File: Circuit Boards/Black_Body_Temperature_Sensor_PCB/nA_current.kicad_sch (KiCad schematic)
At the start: 12 parts, among them Q7 TMUX1112PWR, U2 LM334M, U3 LT1008

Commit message: power simulation
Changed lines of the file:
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@@
-		)
-	)
-	(label "\"sel\"{100na_neg 100na_pos 10na_neg 10na_pos}"
-		(at 162.56 120.65 90)
-		(effects
-			(font
-				(size 0.2 0.2)
-			)
-			(justify left bottom)
 		)
 	)

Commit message: Schematic ready for review
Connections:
- net +4V renamed +3V3A
- net -4V renamed -3V3A

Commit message: Temp sensor schematic done
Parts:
- C301: renamed from C1; footprint (none) -> Capacitor_SMD:C_0603_1608Metric
- R301: renamed from R12; footprint (none) -> Resistor_SMD:R_0603_1608Metric
- R302: renamed from R13; footprint (none) -> Resistor_SMD:R_0603_1608Metric
- R303: renamed from R14; footprint (none) -> Resistor_SMD:R_0603_1608Metric
- R304: renamed from R11; footprint (none) -> Resistor_SMD:R_0603_1608Metric
- R305: renamed from R9; footprint (none) -> Resistor_SMD:R_0603_1608Metric
- R306: renamed from R10; footprint (none) -> Resistor_SMD:R_0603_1608Metric
- R307: renamed from R15; footprint (none) -> Resistor_SMD:R_0603_1608Metric
- renumbered D1 to D301, Q7 to Q301, U2 to U301, U3 to U302
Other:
- note added: "nA Current (PAGE 3)"
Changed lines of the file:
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@@
 	(generator_version "10.0")
 	(paper "A4")
+	(text "nA Current (PAGE 3)"
+		(exclude_from_sim no)
+		(at 69.85 24.13 0)
+		(effects
+			(font
+				(size 7 7)
+			)
+		)
+	)
 	(junction
 		(at 83.82 82.55)
@@
 		(dnp no)
 		(fields_autoplaced yes)
-		(property "Reference" "R9"
+		(property "Reference" "R305"
 			(at 105.41 76.1999 0)
 			(show_name no)
@@
 			)
 		)
-		(property "Footprint" ""
+		(property "Footprint" "Resistor_SMD:R_0603_1608Metric"
 			(at 101.092 77.47 90)
 			(hide yes)
@@
 			(project "Black_Body_Temperature_Sensor_PCB"
 				(path "/e46fba8d-0294-4f4f-927d-8614bb9d51d3/c0a0512b-fc86-46bb-aa4c-7d38a9ff5302"
-					(reference "R9")
+					(reference "R305")
 					(unit 1)
 				)
@@
 		(dnp no)
 		(fields_autoplaced yes)
-		(property "Reference" "R12"
+		(property "Reference" "R301"
 			(at 78.74 86.3599 0)
 			(show_name no)
@@
 			)
 		)
-		(property "Footprint" ""
+		(property "Footprint" "Resistor_SMD:R_0603_1608Metric"
 			(at 74.422 87.63 90)
 			(hide yes)
@@
 			(project "Black_Body_Temperature_Sensor_PCB"
 				(path "/e46fba8d-0294-4f4f-927d-8614bb9d51d3/c0a0512b-fc86-46bb-aa4c-7d38a9ff5302"
-					(reference "R12")
+					(reference "R301")
 					(unit 1)
 				)
@@
 		(dnp no)
 		(fields_autoplaced yes)
-		(property "Reference" "R13"
+		(property "Reference" "R302"
 			(at 86.36 76.1999 0)
 			(show_name no)
@@
 			)
 		)
-		(property "Footprint" ""
+		(property "Footprint" "Resistor_SMD:R_0603_1608Metric"
 			(at 82.042 77.47 90)
 			(hide yes)
@@
 			(project "Black_Body_Temperature_Sensor_PCB"
 				(path "/e46fba8d-0294-4f4f-927d-8614bb9d51d3/c0a0512b-fc86-46bb-aa4c-7d38a9ff5302"
-					(reference "R13")
+					(reference "R302")
 					(unit 1)
 				)
@@
 		(in_pos_files yes)
 		(dnp no)
-		(property "Reference" "C1"
-			(at 167.64 105.41 90)
+		(property "Reference" "C301"
+			(at 168.91 107.95 90)
 			(show_name no)
 			(do_not_autoplace no)
@@
 		)
 		(property "Value" "200pf"
-			(at 167.64 107.95 90)
-			(show_name no)
-			(do_not_autoplace no)
-			(effects
-				(font
-					(size 1.27 1.27)
-				)
-			)
-		)
-		(property "Footprint" ""
+			(at 168.91 110.49 90)
+			(show_name no)
+			(do_not_autoplace no)
+			(effects
+				(font
+					(size 1.27 1.27)
+				)
+			)
+		)
+		(property "Footprint" "Capacitor_SMD:C_0603_1608Metric"
 			(at 173.99 103.1748 0)
 			(hide yes)
@@
 			(project "Black_Body_Temperature_Sensor_PCB"
 				(path "/e46fba8d-0294-4f4f-927d-8614bb9d51d3/c0a0512b-fc86-46bb-aa4c-7d38a9ff5302"
-					(reference "C1")
+					(reference "C301")
 					(unit 1)
 				)
@@
 		(dnp no)
 		(fields_autoplaced yes)
-		(property "Reference" "R14"
+		(property "Reference" "R303"
 			(at 86.36 86.3599 0)
 			(show_name no)
@@
 			)
 		)
-		(property "Footprint" ""
+		(property "Footprint" "Resistor_SMD:R_0603_1608Metric"
 			(at 82.042 87.63 90)
 			(hide yes)
@@
 			(project "Black_Body_Temperature_Sensor_PCB"
 				(path "/e46fba8d-0294-4f4f-927d-8614bb9d51d3/c0a0512b-fc86-46bb-aa4c-7d38a9ff5302"
-					(reference "R14")
+					(reference "R303")
 					(unit 1)
 				)
@@
 		(dnp no)
 		(fields_autoplaced yes)
-		(property "Reference" "R15"
+		(property "Reference" "R307"
 			(at 163.83 77.4699 0)
 			(show_name no)
@@
 			)
 		)
-		(property "Footprint" ""
+		(property "Footprint" "Resistor_SMD:R_0603_1608Metric"
 			(at 159.512 78.74 90)
 			(hide yes)
@@
 			(project "Black_Body_Temperature_Sensor_PCB"
 				(path "/e46fba8d-0294-4f4f-927d-8614bb9d51d3/c0a0512b-fc86-46bb-aa4c-7d38a9ff5302"
-					(reference "R15")
+					(reference "R307")
 					(unit 1)
 				)
@@
 		(dnp no)
 		(fields_autoplaced yes)
-		(property "Reference" "R10"
+		(property "Reference" "R306"
 			(at 105.41 86.3599 0)
 			(show_name no)
@@
 			)
 		)
-		(property "Footprint" ""
+		(property "Footprint" "Resistor_SMD:R_0603_1608Metric"
 			(at 101.092 87.63 90)
 			(hide yes)
@@
 			(project "Black_Body_Temperature_Sensor_PCB"
 				(path "/e46fba8d-0294-4f4f-927d-8614bb9d51d3/c0a0512b-fc86-46bb-aa4c-7d38a9ff5302"
-					(reference "R10")
+					(reference "R306")
 					(unit 1)
 				)
@@
 		(dnp no)
 		(fields_autoplaced yes)
-		(property "Reference" "R11"
+		(property "Reference" "R304"
 			(at 96.52 86.3599 0)
 			(show_name no)
@@
 			)
 		)
-		(property "Footprint" ""
+		(property "Footprint" "Resistor_SMD:R_0603_1608Metric"
 			(at 92.202 87.63 90)
 			(hide yes)
@@
 			(project "Black_Body_Temperature_Sensor_PCB"
 				(path "/e46fba8d-0294-4f4f-927d-8614bb9d51d3/c0a0512b-fc86-46bb-aa4c-7d38a9ff5302"
-					(reference "R11")
+					(reference "R304")
 					(unit 1)
 				)
@@
 		(dnp no)
 		(fields_autoplaced yes)
-		(property "Reference" "U2"
+		(property "Reference" "U301"
 			(at 148.59 73.3424 0)
 			(show_name no)
@@
 			(project "Black_Body_Temperature_Sensor_PCB"
 				(path "/e46fba8d-0294-4f4f-927d-8614bb9d51d3/c0a0512b-fc86-46bb-aa4c-7d38a9ff5302"
-					(reference "U2")
+					(reference "U301")
 					(unit 1)
 				)
@@
 		(in_pos_files yes)
 		(dnp no)
-		(property "Reference" "D1"
+		(property "Reference" "D301"
 			(at 152.4 86.36 90)
 			(show_name no)
@@
 			(project "Black_Body_Temperature_Sensor_PCB"
 				(path "/e46fba8d-0294-4f4f-927d-8614bb9d51d3/c0a0512b-fc86-46bb-aa4c-7d38a9ff5302"
-					(reference "D1")
+					(reference "D301")
 					(unit 1)
 				)
@@
 		(in_pos_files yes)
 		(dnp no)
-		(property "Reference" "#PWR07"
+		(property "Reference" "#PWR0305"
 			(at 175.26 100.33 0)
 			(hide yes)
@@
 			(project "Black_Body_Temperature_Sensor_PCB"
 				(path "/e46fba8d-0294-4f4f-927d-8614bb9d51d3/c0a0512b-fc86-46bb-aa4c-7d38a9ff5302"
-					(reference "#PWR07")
+					(reference "#PWR0305")
 					(unit 1)
 				)
@@
 		(in_pos_files yes)
 		(dnp no)
-		(property "Reference" "U3"
+		(property "Reference" "U302"
 			(at 175.26 90.17 0)
 			(show_name no)
@@
 			(project "Black_Body_Temperature_Sensor_PCB"
 				(path "/e46fba8d-0294-4f4f-927d-8614bb9d51d3/c0a0512b-fc86-46bb-aa4c-7d38a9ff5302"
-					(reference "U3")
+					(reference "U302")
 					(unit 1)
 				)
@@
 		(in_pos_files yes)
 		(dnp no)
-		(property "Reference" "#PWR06"
+		(property "Reference" "#PWR0304"
 			(at 170.18 95.25 0)
 			(hide yes)
@@
 			(project "Black_Body_Temperature_Sensor_PCB"
 				(path "/e46fba8d-0294-4f4f-927d-8614bb9d51d3/c0a0512b-fc86-46bb-aa4c-7d38a9ff5302"
-					(reference "#PWR06")
+					(reference "#PWR0304")
 					(unit 1)
 				)
@@
 		(dnp no)
 		(fields_autoplaced yes)
-		(property "Reference" "#PWR08"
+		(property "Reference" "#PWR0303"
 			(at 152.4 73.66 0)
 			(hide yes)
@@
 			(project "Black_Body_Temperature_Sensor_PCB"
 				(path "/e46fba8d-0294-4f4f-927d-8614bb9d51d3/c0a0512b-fc86-46bb-aa4c-7d38a9ff5302"
-					(reference "#PWR08")
+					(reference "#PWR0303")
 					(unit 1)
 				)
@@
 		(dnp no)
 		(fields_autoplaced yes)
-		(property "Reference" "#PWR09"
+		(property "Reference" "#PWR0301"
 			(at 137.16 92.71 0)
 			(hide yes)
@@
 			(project "Black_Body_Temperature_Sensor_PCB"
 				(path "/e46fba8d-0294-4f4f-927d-8614bb9d51d3/c0a0512b-fc86-46bb-aa4c-7d38a9ff5302"
-					(reference "#PWR09")
+					(reference "#PWR0301")
 					(unit 1)
 				)
@@
 		(in_pos_files yes)
 		(dnp no)
-		(property "Reference" "Q7"
+		(property "Reference" "Q301"
 			(at 120.65 86.36 0)
 			(show_name no)
@@
 			(project "Black_Body_Temperature_Sensor_PCB"
 				(path "/e46fba8d-0294-4f4f-927d-8614bb9d51d3/c0a0512b-fc86-46bb-aa4c-7d38a9ff5302"
-					(reference "Q7")
+					(reference "Q301")
 					(unit 1)
 				)
@@
 		(dnp no)
 		(fields_autoplaced yes)
-		(property "Reference" "#PWR010"
+		(property "Reference" "#PWR0302"
 			(at 137.16 124.46 0)
 			(hide yes)
@@
 			(project "Black_Body_Temperature_Sensor_PCB"
 				(path "/e46fba8d-0294-4f4f-927d-8614bb9d51d3/c0a0512b-fc86-46bb-aa4c-7d38a9ff5302"
-					(reference "#PWR010")
+					(reference "#PWR0302")
 					(unit 1)
 				)

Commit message: temp pcb analog layout done
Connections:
- net 100na_neg: now also Q301.14 (S2); no longer Q301.3 (S1)
- net 10na_neg: now also Q301.3 (S1); no longer Q301.14 (S2)
- net 10na: now reaches R304.1, R305.2, R306.1
- net 100na: now reaches R301.1, R302.2, R303.1
- net fb: now reaches R307.1, U301.1
- net feedback: now reaches D301.4, Q301.15 (D2), Q301.2 (D1), U302.2 (-), U302.6
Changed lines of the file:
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@@
-	)
-	(junction
-		(at 152.4 93.98)
-		(diameter 0)
-		(color 0 0 0 0)
 	)
 	(junction
@@
 	)
 	(junction
+		(at 148.59 93.98)
+		(diameter 0)
+		(color 0 0 0 0)
+	)
+	(junction
 		(at 157.48 93.98)
 		(diameter 0)
@@
 	(wire
 		(pts
+			(xy 148.59 93.98) (xy 157.48 93.98)
+		)
+		(stroke
+			(width 0)
+			(type default)
+		)
+	)
+	(wire
+		(pts
 			(xy 93.98 101.6) (xy 127 101.6)
 		)
@@
 	(wire
 		(pts
-			(xy 152.4 93.98) (xy 157.48 93.98)
-		)
-		(stroke
-			(width 0)
-			(type default)
-		)
-	)
-	(wire
-		(pts
 			(xy 102.87 82.55) (xy 102.87 83.82)
 		)
@@
 	(wire
 		(pts
-			(xy 147.32 93.98) (xy 152.4 93.98)
+			(xy 147.32 93.98) (xy 148.59 93.98)
 		)
 		(stroke
@@
 	(wire
 		(pts
-			(xy 83.82 93.98) (xy 127 93.98)
-		)
-		(stroke
-			(width 0)
-			(type default)
-		)
-	)
-	(wire
-		(pts
 			(xy 157.48 92.71) (xy 157.48 93.98)
 		)
@@
 	(wire
 		(pts
-			(xy 152.4 96.52) (xy 152.4 93.98)
+			(xy 148.59 96.52) (xy 148.59 93.98)
 		)
 		(stroke
@@
 	(wire
 		(pts
-			(xy 102.87 91.44) (xy 102.87 96.52)
+			(xy 102.87 91.44) (xy 102.87 93.98)
 		)
 		(stroke
@@
 	(wire
 		(pts
+			(xy 102.87 93.98) (xy 127 93.98)
+		)
+		(stroke
+			(width 0)
+			(type default)
+		)
+	)
+	(wire
+		(pts
 			(xy 157.48 93.98) (xy 162.56 93.98)
 		)
@@
 	(wire
 		(pts
-			(xy 83.82 91.44) (xy 83.82 93.98)
+			(xy 83.82 91.44) (xy 83.82 96.52)
 		)
 		(stroke
@@
 	(wire
 		(pts
-			(xy 102.87 96.52) (xy 127 96.52)
-		)
-		(stroke
-			(width 0)
-			(type default)
-		)
-	)
-	(wire
-		(pts
 			(xy 165.1 104.14) (xy 166.37 104.14)
 		)
@@
 	(wire
 		(pts
+			(xy 83.82 96.52) (xy 127 96.52)
+		)
+		(stroke
+			(width 0)
+			(type default)
+		)
+	)
+	(wire
+		(pts
 			(xy 160.02 111.76) (xy 147.32 111.76)
 		)
@@
 	(wire
 		(pts
-			(xy 147.32 96.52) (xy 152.4 96.52)
+			(xy 147.32 96.52) (xy 148.59 96.52)
 		)
 		(stroke
@@
 		)
 	)
-	(label "100na_neg"
+	(label "fb"
+		(at 157.48 74.93 0)
+		(effects
+			(font
+				(size 1.27 1.27)
+			)
+			(justify left bottom)
+		)
+	)
+	(label "10na_neg"
 		(at 115.57 93.98 0)
 		(effects
@@
 		)
 	)
-	(label "10na_neg"
+	(label "100na_neg"
 		(at 115.57 96.52 0)
 		(effects
@@
 		)
 	)
+	(label "100na"
+		(at 76.2 82.55 0)
+		(effects
+			(font
+				(size 1.27 1.27)
+			)
+			(justify left bottom)
+		)
+	)
 	(label "10na_pos"
 		(at 115.57 101.6 0)
@@
 		)
 	)
+	(label "10na"
+		(at 95.25 82.55 0)
+		(effects
+			(font
+				(size 1.27 1.27)
+			)
+			(justify left bottom)
+		)
+	)
+	(label "feedback"
+		(at 148.59 93.98 0)
+		(effects
+			(font
+				(size 1.27 1.27)
+			)
+			(justify left bottom)
+		)
+	)

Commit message: Complete except for recommended changes
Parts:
- added C301, C302, C303, C304, C305, C306, C307, C308: 2u2, Capacitor_SMD:C_0402_1005Metric, symbol Device:C
- added R301, R302, R303, R304: 5.1k, Resistor_SMD:R_0402_1005Metric, symbol Device:R
- renumbered C301 to C309, R301 to R305, R302 to R306, R303 to R307, R304 to R308, R305 to R309, R306 to R310, R307 to R311
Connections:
- net GNDPWR: now also C301.2, C302.2, C303.2, C304.2, C305.2, C306.2, C307.2, C308.2
- net sel.100na_neg: now also C306.1, R302.2; no longer Q301.1 (SEL1)
- net sel.100na_pos: now also C307.1, R303.2; no longer Q301.9 (SEL3)
- net sel.10na_neg: now also C305.1, R301.2; no longer Q301.16 (SEL2)
- net sel.10na_pos: now also C308.1, R304.2; no longer Q301.8 (SEL4)
- new net sel1: C301.1, Q301.1 (SEL1), R301.1
- new net sel2: C302.1, Q301.16 (SEL2), R302.1
- new net sel3: C303.1, Q301.9 (SEL3), R303.1
- new net sel4: C304.1, Q301.8 (SEL4), R304.1

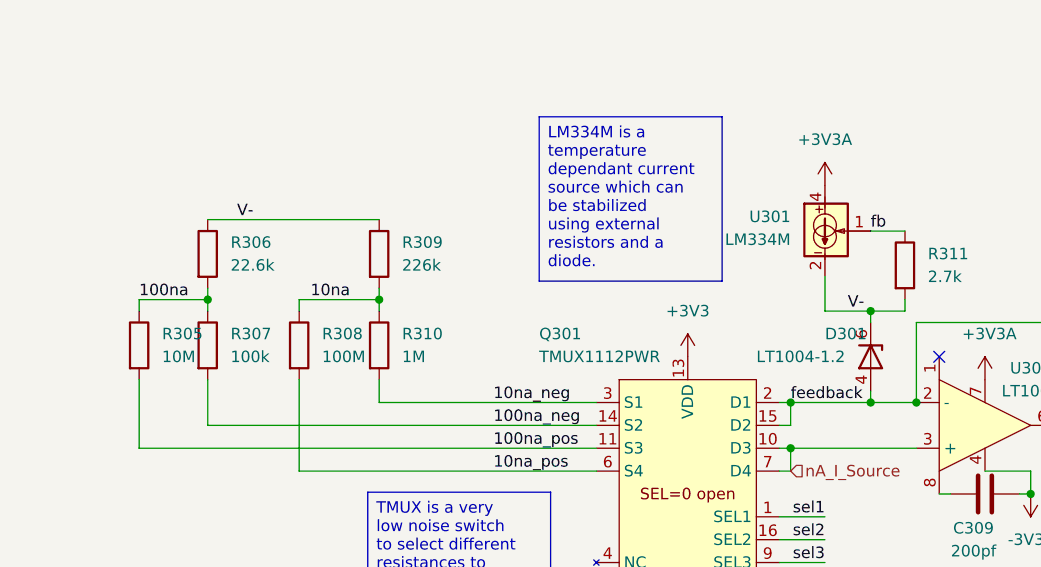
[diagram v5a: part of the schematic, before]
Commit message: Temp probe bom done
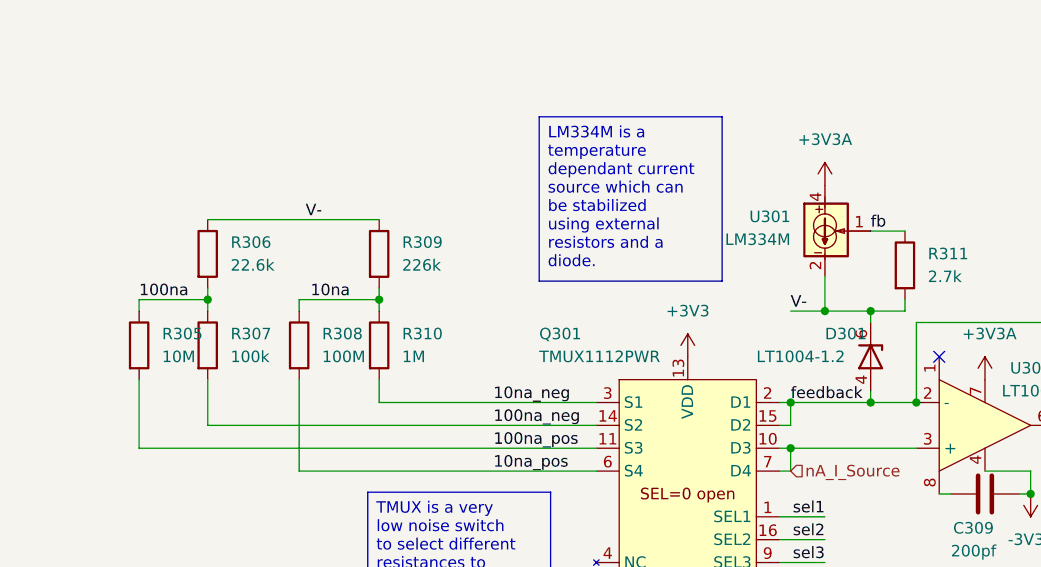
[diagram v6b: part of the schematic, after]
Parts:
- C301, C302, C303, C304, C305, C306, C307, C308: MPN (none) -> GRM155R61E225ME15D
- C309: MPN (none) -> CL10C201JB8NNNC
- D301: MPN (none) -> LT1004-1.2
- Q301: MPN (none) -> TMUX1112PWR
- R301, R302, R303, R304: MPN (none) -> RT0402BRD075K1L
- R305: MPN (none) -> CRCW060310M0DHEAP
- R306: MPN (none) -> ERA-3AEB2262V
- R307: MPN (none) -> ERA-3AEB104V; now in the parts list
- R308: MPN (none) -> HVC0603T1006FET
- R309: MPN (none) -> ERA-3AEB2263V
- R310: MPN (none) -> RN73H1JTTD1004B25
- R311: MPN (none) -> ERA-3AEB272V
- U301: MPN (none) -> LM334M
- U302: MPN (none) -> LT1008

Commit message: Designs finished - order placed
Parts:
- D301: MPN LT1004-1.2 -> LT1004CS8-1.2#TRPBF
- U302: MPN LT1008 -> LT1008S8#PBF
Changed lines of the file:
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@@
 			)
 		)
-		(property "MPN" "LT1004-1.2"
+		(property "MPN" "LT1004CS8-1.2#TRPBF"
 			(at 157.48 87.63 90)
 			(hide yes)
@@
 			)
 		)
-		(property "MPN" "LT1008"
+		(property "MPN" "LT1008S8#PBF"
 			(at 170.18 96.52 0)
 			(hide yes)
